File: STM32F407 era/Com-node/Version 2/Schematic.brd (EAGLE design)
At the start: 127 x 165.1 mm, 83 parts, among them IC2 lm2575, Q2 12MHz, Q3 12MHz, U1 MAX13052ESA+, U2 SMS05, U3 MAX232AEWE+, X1 SDBMF, X5 679105700

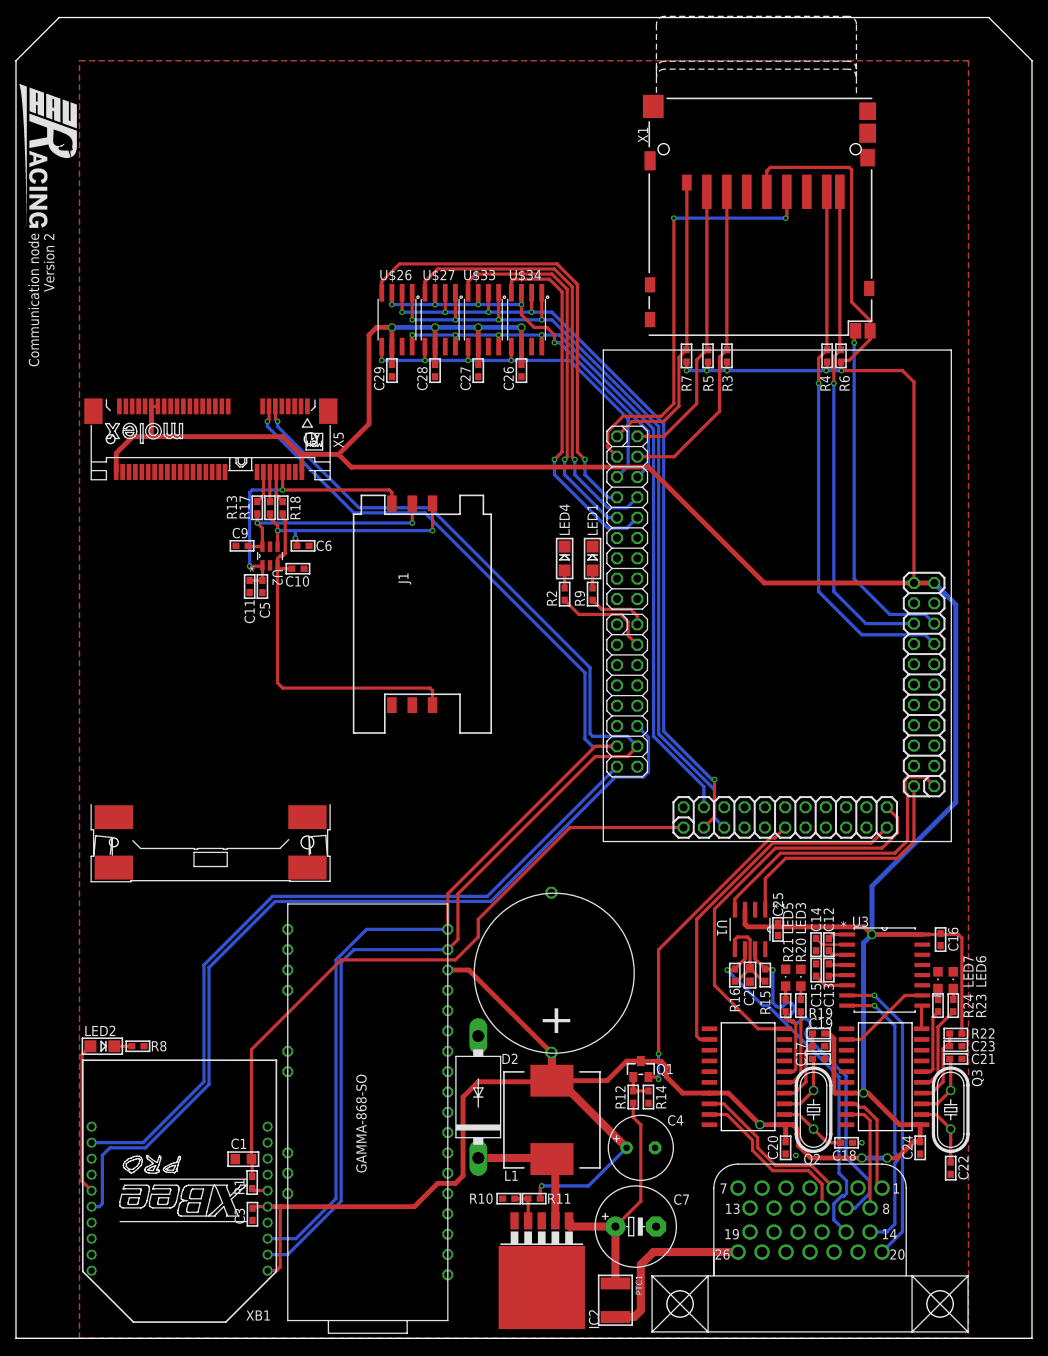
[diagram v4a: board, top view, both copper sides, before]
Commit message: fixed minor mistakes, added GPS header
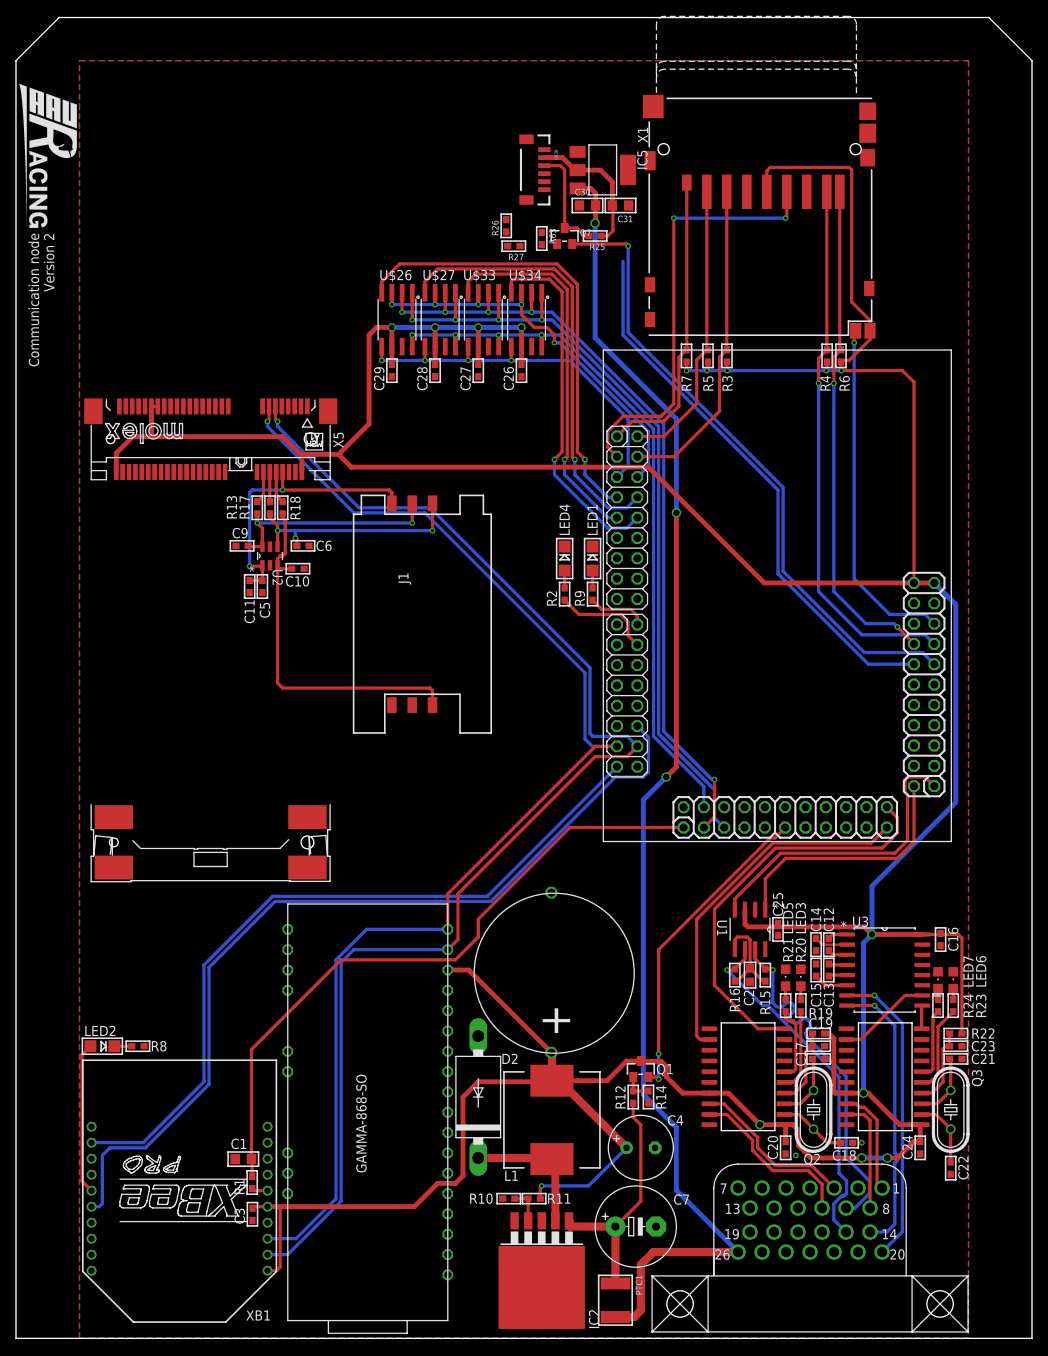
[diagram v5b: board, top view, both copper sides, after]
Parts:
- added C30: 10u, microbuilder:_0805
- added C31: 22u, microbuilder:_0805
- added IC5: REG1117, burr-brown:SOT223
- added Q7: (no value), microbuilder:SOT23-WIDE
- added R25, R63: 500, microbuilder:_0603
- added R26: 499, microbuilder:_0603
- added R27: 976, microbuilder:_0603
- added U$36: EM406, SparkFun:EM406
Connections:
- new net 5.0V: C31.2, IC5.2, R25.1, U$36.2
- new net GPS_RX: R26.1, R27.2, U$1.P$36
- new net GPS_TX: Q7.2, U$1.P$35
- new net N$58: Q7.1, R63.2
- new net RXD1: R26.2, U$36.4
- new net TXD1: Q7.3, R25.2, U$36.3
- net 12V: now also C30.2, IC5.3
- net 3.3V: now also R63.1
- net GND: now also C30.1, C31.1, IC5.1, R27.1, U$36.1, U$36.5
- net SDIO_D1: now also U$1.P$38; no longer U$1.P$40
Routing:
- net 12V: track 22.0 -> 167.7 mm, vias 0 -> 3
- net GPS_TX: track 0.00 -> 79.5 mm, vias 0 -> 1
- net GPS_RX: track 0.00 -> 68.8 mm
- net 5.0V: track 0.00 -> 17.6 mm
- net TXD1: track 0.00 -> 13.5 mm
- net SDIO_D1: track 62.1 -> 63.2 mm, vias 1 -> 2
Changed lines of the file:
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@@
 <attribute name="VALUE" x="48.4823" y="119.6975" size="0.4064" layer="27" ratio="10" rot="R90"/>
 </element>
+<element name="U$36" library="SparkFun" package="EM406" value="EM406" x="66.04" y="148.59" rot="R270"/>
+<element name="IC5" library="burr-brown" package="SOT223" value="REG1117" x="73.3425" y="146.05" rot="R270">
+<attribute name="OC_NEWARK" value="14P6981" x="86.0425" y="154.6225" size="1.778" layer="27" rot="R270" display="off"/>
+<attribute name="MPN" value="REG1117" x="86.0425" y="154.6225" size="1.778" layer="27" rot="R270" display="off"/>
+<attribute name="MF" value="" x="86.0425" y="154.6225" size="1.778" layer="27" rot="R270" display="off"/>
+<attribute name="OC_FARNELL" value="1097566" x="86.0425" y="154.6225" size="1.778" layer="27" rot="R270" display="off"/>
+</element>
+<element name="C30" library="microbuilder" package="_0805" value="10u" x="71.4375" y="141.605"/>
+<element name="C31" library="microbuilder" package="_0805" value="22u" x="75.565" y="141.605" rot="R180"/>
+<element name="Q7" library="microbuilder" package="SOT23-WIDE" value="" x="68.58" y="137.795"/>
+<element name="R25" library="microbuilder" package="_0603" value="500" x="72.39" y="137.795" rot="R180"/>
+<element name="R63" library="microbuilder" package="_0603" value="500" x="65.7225" y="137.4775" rot="R270"/>
+<element name="R26" library="microbuilder" package="_0603" value="499" x="61.2775" y="139.065" rot="R90"/>
+<element name="R27" library="microbuilder" package="_0603" value="976" x="62.23" y="136.525" rot="R180"/>
 </elements>
 <signals>
@@
 </signal>
 <signal name="SDIO_D1">
-<contactref element="U$1" pad="P$40"/>
 <contactref element="X1" pad="8"/>
 <contactref element="R6" pad="2"/>
@@
 <wire x1="103.1194" y1="123.5693" x2="102.235" y2="122.6849" width="0.4064" layer="1"/>
 <wire x1="102.235" y1="122.6849" x2="102.235" y2="119.38" width="0.4064" layer="1"/>
-<wire x1="112.24745" y1="89.34215" x2="106.23785" y2="89.34215" width="0.4064" layer="16"/>
 <wire x1="106.23785" y1="89.34215" x2="102.235" y2="93.345" width="0.4064" layer="16"/>
 <wire x1="102.235" y1="93.345" x2="102.235" y2="119.38" width="0.4064" layer="16"/>
 <via x="102.235" y="119.38" extent="1-16" drill="0.381"/>
+<contactref element="U$1" pad="P$38"/>
+<wire x1="106.23785" y1="89.34215" x2="109.73035" y2="89.34215" width="0.4064" layer="16"/>
+<wire x1="109.73035" y1="89.34215" x2="110.1725" y2="88.9" width="0.4064" layer="16"/>
+<via x="110.1725" y="88.9" extent="1-16" drill="0.381"/>
+<wire x1="110.1725" y1="88.9" x2="112.24745" y2="86.82505" width="0.4064" layer="1"/>
+<wire x1="112.24745" y1="86.82505" x2="112.24745" y2="86.80215" width="0.4064" layer="1"/>
 </signal>
 <signal name="USART1_RX">
@@
 <via x="105.7275" y="24.4475" extent="1-16" drill="0.381"/>
 <via x="97.4725" y="22.86" extent="1-16" drill="0.381"/>
+<contactref element="U$36" pad="5"/>
+<contactref element="U$36" pad="1"/>
+<contactref element="IC5" pad="1"/>
+<contactref element="IC5" pad="1"/>
+<contactref element="C30" pad="1"/>
+<contactref element="C31" pad="1"/>
+<contactref element="R27" pad="1"/>
+<wire x1="70.4215" y1="141.605" x2="66.04" y2="144.59" width="0" layer="19" extent="1-1"/>
 </signal>
 <signal name="3.3V">
@@
 <wire x1="110.1725" y1="22.5425" x2="112.2045" y2="24.5745" width="0.6096" layer="1"/>
 <wire x1="112.2045" y1="24.5745" x2="113.03" y2="24.5745" width="0.6096" layer="1"/>
+<contactref element="R63" pad="1"/>
+<wire x1="63.1825" y1="126.365" x2="65.7225" y2="138.2395" width="0" layer="19" extent="1-1"/>
 </signal>
 <signal name="N$1">
@@
 <wire x1="78.105" y1="3.4925" x2="77.275" y2="2.6625" width="1.016" layer="1"/>
 <wire x1="77.275" y1="2.6625" x2="74.93" y2="2.6625" width="1.016" layer="1"/>
+<contactref element="IC5" pad="3"/>
+<contactref element="C30" pad="2"/>
+<wire x1="70.1929" y1="143.7386" x2="71.8439" y2="143.7386" width="0.6096" layer="1"/>
+<wire x1="71.8439" y1="143.7386" x2="72.4535" y2="143.129" width="0.6096" layer="1"/>
+<wire x1="72.4535" y1="143.129" x2="72.4535" y2="141.605" width="0.6096" layer="1"/>
+<wire x1="90.2575" y1="10.7875" x2="82.55" y2="18.495" width="0.6096" layer="16"/>
+<wire x1="82.55" y1="18.495" x2="82.55" y2="26.3525" width="0.6096" layer="16"/>
+<wire x1="82.55" y1="26.3525" x2="78.4225" y2="30.48" width="0.6096" layer="16"/>
+<wire x1="78.4225" y1="30.48" x2="78.4225" y2="67.31" width="0.6096" layer="16"/>
+<wire x1="78.4225" y1="67.31" x2="81.28" y2="70.1675" width="0.6096" layer="16"/>
+<via x="81.28" y="70.1675" extent="1-16" drill="0.8"/>
+<wire x1="81.28" y1="70.1675" x2="82.55" y2="71.4375" width="0.6096" layer="1"/>
+<wire x1="82.55" y1="71.4375" x2="82.55" y2="103.1875" width="0.6096" layer="1"/>
+<via x="82.55" y="103.1875" extent="1-16" drill="0.8"/>
+<wire x1="82.55" y1="103.1875" x2="82.55" y2="114.935" width="0.6096" layer="16"/>
+<wire x1="82.55" y1="114.935" x2="72.39" y2="125.095" width="0.6096" layer="16"/>
+<wire x1="72.39" y1="125.095" x2="72.39" y2="139.3825" width="0.6096" layer="16"/>
+<via x="72.39" y="139.3825" extent="1-16" drill="0.8"/>
+<wire x1="72.39" y1="139.3825" x2="72.4535" y2="139.446" width="0.6096" layer="1"/>
+<wire x1="72.4535" y1="139.446" x2="72.4535" y2="141.605" width="0.6096" layer="1"/>
 </signal>
 <signal name="COMRX">
@@
 </signal>
 <signal name="N$123">
-</signal>
-<signal name="ECU2L">
 </signal>
 <signal name="HB-EN2">
@@
 <wire x1="76.3723" y1="101.2825" x2="77.6717" y2="102.5819" width="0.4064" layer="16"/>
 </signal>
+<signal name="TXD1">
+<contactref element="U$36" pad="3"/>
+<contactref element="Q7" pad="3"/>
+<contactref element="R25" pad="2"/>
+<wire x1="71.628" y1="137.795" x2="71.12" y2="137.795" width="0.4064" layer="1"/>
+<wire x1="71.12" y1="137.795" x2="70.12" y2="138.795" width="0.4064" layer="1"/>
+<wire x1="70.12" y1="138.795" x2="68.58" y2="138.795" width="0.4064" layer="1"/>
+<wire x1="68.58" y1="138.795" x2="68.58" y2="146.05" width="0.4064" layer="1"/>
+<wire x1="68.58" y1="146.05" x2="68.04" y2="146.59" width="0.4064" layer="1"/>
+<wire x1="68.04" y1="146.59" x2="66.04" y2="146.59" width="0.4064" layer="1"/>
+</signal>
+<signal name="RXD1">
+<contactref element="U$36" pad="4"/>
+<contactref element="R26" pad="2"/>
+<wire x1="61.2775" y1="139.827" x2="66.04" y2="145.59" width="0" layer="19" extent="1-1"/>
+</signal>
+<signal name="GPS_RX">
+<contactref element="U$1" pad="P$36"/>
+<contactref element="R26" pad="1"/>
+<contactref element="R27" pad="2"/>
+<wire x1="112.24745" y1="84.26215" x2="106.55535" y2="84.26215" width="0.4064" layer="16"/>
+<wire x1="106.55535" y1="84.26215" x2="95.25" y2="95.5675" width="0.4064" layer="16"/>
+<wire x1="95.25" y1="95.5675" x2="95.25" y2="106.045" width="0.4064" layer="16"/>
+<wire x1="95.25" y1="106.045" x2="75.8825" y2="125.4125" width="0.4064" layer="16"/>
+<wire x1="75.8825" y1="125.4125" x2="75.8825" y2="134.62" width="0.4064" layer="16"/>
+<wire x1="61.468" y1="136.525" x2="61.2775" y2="138.303" width="0" layer="19" extent="1-1"/>
+<wire x1="75.8825" y1="134.62" x2="61.468" y2="136.525" width="0" layer="19" extent="1-16"/>
+</signal>
+<signal name="GPS_TX">
+<contactref element="U$1" pad="P$35"/>
+<contactref element="Q7" pad="2"/>
+<wire x1="114.78745" y1="84.26215" x2="113.3246" y2="85.725" width="0.4064" layer="16"/>
+<wire x1="113.3246" y1="85.725" x2="106.045" y2="85.725" width="0.4064" layer="16"/>
+<wire x1="106.045" y1="85.725" x2="95.885" y2="95.885" width="0.4064" layer="16"/>
+<wire x1="95.885" y1="95.885" x2="95.885" y2="106.3625" width="0.4064" layer="16"/>
+<wire x1="95.885" y1="106.3625" x2="76.5175" y2="125.73" width="0.4064" layer="16"/>
+<wire x1="76.5175" y1="125.73" x2="76.5175" y2="136.525" width="0.4064" layer="16"/>
+<wire x1="69.53" y1="136.795" x2="76.2475" y2="136.795" width="0.4064" layer="1"/>
+<wire x1="76.2475" y1="136.795" x2="76.5175" y2="136.525" width="0.4064" layer="1"/>
+<via x="76.5175" y="136.525" extent="1-16" drill="0.381"/>
+</signal>
+<signal name="5.0V">
+<contactref element="U$36" pad="2"/>
+<contactref element="IC5" pad="2"/>
+<contactref element="C31" pad="2"/>
+<wire x1="70.1929" y1="146.0246" x2="73.0504" y2="146.0246" width="0.6096" layer="1"/>
+<wire x1="73.0504" y1="146.0246" x2="74.549" y2="144.526" width="0.6096" layer="1"/>
+<wire x1="74.549" y1="144.526" x2="74.549" y2="141.605" width="0.6096" layer="1"/>
+<contactref element="R25" pad="1"/>
+<wire x1="66.04" y1="147.59" x2="68.31" y2="147.59" width="0.6096" layer="1"/>
+<wire x1="68.31" y1="147.59" x2="69.5325" y2="146.3675" width="0.6096" layer="1"/>
+<wire x1="69.5325" y1="146.3675" x2="69.85" y2="146.3675" width="0.6096" layer="1"/>
+<wire x1="69.85" y1="146.3675" x2="70.1929" y2="146.0246" width="0.6096" layer="1"/>
+<wire x1="73.152" y1="137.795" x2="73.9775" y2="137.795" width="0.4064" layer="1"/>
+<wire x1="73.9775" y1="137.795" x2="74.6125" y2="138.43" width="0.4064" layer="1"/>
+<wire x1="74.6125" y1="138.43" x2="74.6125" y2="141.5415" width="0.4064" layer="1"/>
+<wire x1="74.6125" y1="141.5415" x2="74.549" y2="141.605" width="0.4064" layer="1"/>
+</signal>
+<signal name="N$58">
+<contactref element="Q7" pad="1"/>
+<contactref element="R63" pad="2"/>
+<wire x1="65.7225" y1="136.7155" x2="67.63" y2="136.795" width="0" layer="19" extent="1-1"/>
+</signal>
 </signals>
-<errors>
-</errors>
 </board>
 </drawing>
